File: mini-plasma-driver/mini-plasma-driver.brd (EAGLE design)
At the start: 100 x 80 mm, 92 parts, among them IC1 IR21844D, IC2 74LS19N, IC3 NE555N, IC5 IR21844D, J1 12v IN, Q1 STH60N10W, Q3 2N2369, Q4 2N2369, Q7 STH60N10W, Q8 STH60N10W, Q9 STH60N10W

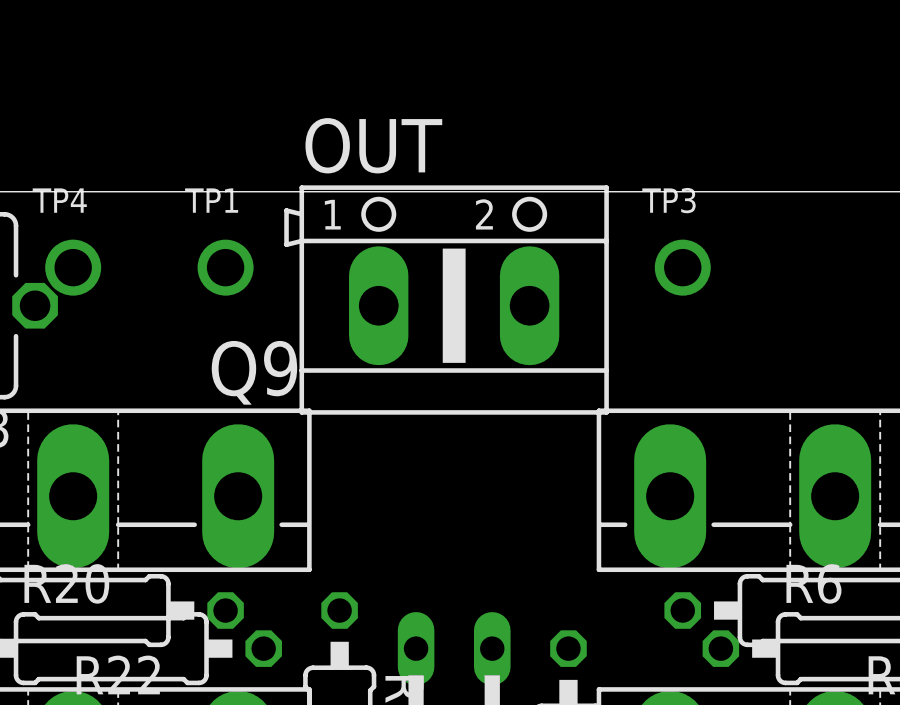
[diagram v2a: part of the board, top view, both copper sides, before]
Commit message: rotate out connector so that wires dont cross eachother
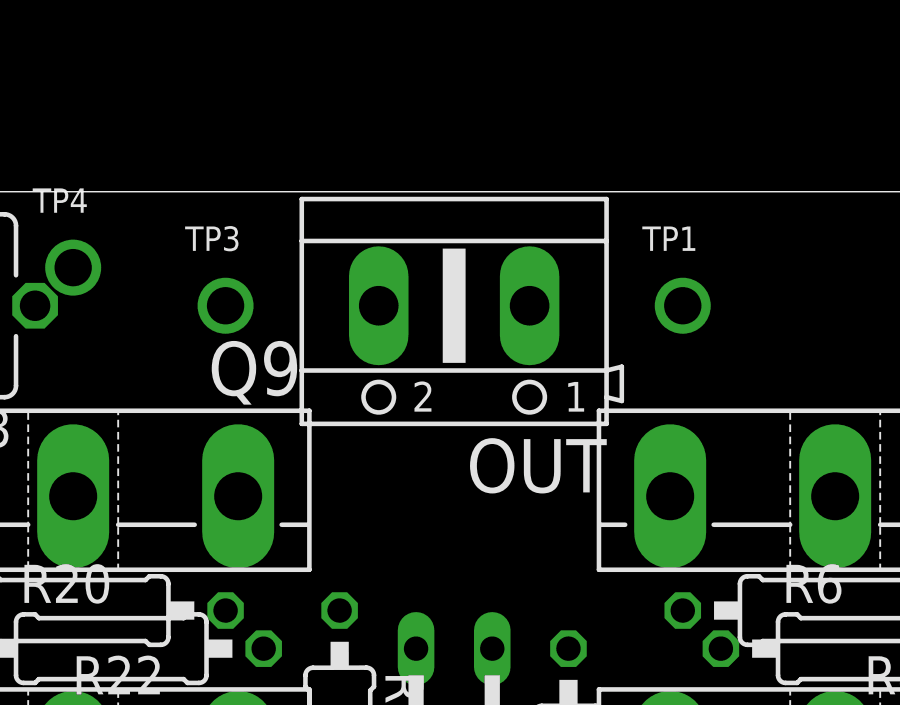
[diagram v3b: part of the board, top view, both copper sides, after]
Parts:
- moved TP1 15.3 mm to (71.1, 76.2)
- moved TP3 15.3 mm to (55.9, 76.2)
- turned OUT to 180 degrees
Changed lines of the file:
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@@
 <attribute name="OC_NEWARK" value="unknown" x="13.97" y="5.08" size="1.778" layer="28" rot="MR180" display="off"/>
 </element>
-<element name="OUT" library="con-ptr500" library_urn="urn:adsk.eagle:library:181" package="AK500/2" package3d_urn="urn:adsk.eagle:package:9880/1" value="" x="63.5" y="76.2">
-<attribute name="MF" value="" x="63.5" y="76.2" size="1.778" layer="27" display="off"/>
-<attribute name="MPN" value="" x="63.5" y="76.2" size="1.778" layer="27" display="off"/>
-<attribute name="OC_FARNELL" value="unknown" x="63.5" y="76.2" size="1.778" layer="27" display="off"/>
-<attribute name="OC_NEWARK" value="unknown" x="63.5" y="76.2" size="1.778" layer="27" display="off"/>
+<element name="OUT" library="con-ptr500" library_urn="urn:adsk.eagle:library:181" package="AK500/2" package3d_urn="urn:adsk.eagle:package:9880/1" value="" x="63.5" y="76.2" rot="R180">
+<attribute name="MF" value="" x="63.5" y="76.2" size="1.778" layer="27" rot="R180" display="off"/>
+<attribute name="MPN" value="" x="63.5" y="76.2" size="1.778" layer="27" rot="R180" display="off"/>
+<attribute name="OC_FARNELL" value="unknown" x="63.5" y="76.2" size="1.778" layer="27" rot="R180" display="off"/>
+<attribute name="OC_NEWARK" value="unknown" x="63.5" y="76.2" size="1.778" layer="27" rot="R180" display="off"/>
 </element>
 <element name="Q3" library="transistor-npn" library_urn="urn:adsk.eagle:library:398" package="TO18" package3d_urn="urn:adsk.eagle:package:28973/2" value="2N2369" x="77.47" y="8.89"/>
@@
 <attribute name="OC_NEWARK" value="29M3118" x="11.43" y="62.23" size="1.778" layer="27" rot="R180" display="off"/>
 </element>
-<element name="TP1" library="microbuilder" package="1X01_ROUND" value="" x="55.88" y="77.47">
-<attribute name="BOM" value="EXCLUDE" x="55.88" y="77.47" size="1.778" layer="27" display="off"/>
+<element name="TP1" library="microbuilder" package="1X01_ROUND" value="" x="71.12" y="76.2">
+<attribute name="BOM" value="EXCLUDE" x="71.12" y="76.2" size="1.778" layer="27" display="off"/>
 </element>
 <element name="TP11" library="microbuilder" package="1X01_ROUND" value="" x="7.62" y="77.47">
@@
 <attribute name="BOM" value="EXCLUDE" x="76.2" y="3.81" size="1.778" layer="27" display="off"/>
 </element>
-<element name="TP3" library="microbuilder" package="1X01_ROUND" value="" x="71.12" y="77.47">
-<attribute name="BOM" value="EXCLUDE" x="71.12" y="77.47" size="1.778" layer="27" display="off"/>
+<element name="TP3" library="microbuilder" package="1X01_ROUND" value="" x="55.88" y="76.2">
+<attribute name="BOM" value="EXCLUDE" x="55.88" y="76.2" size="1.778" layer="27" display="off"/>
 </element>
 <element name="TP4" library="microbuilder" package="1X01_ROUND" value="" x="50.8" y="77.47">
@@
 <wire x1="80.01" y1="45.72" x2="83.82" y2="49.53" width="0" layer="19" extent="1-1"/>
 <wire x1="76.2" y1="69.85" x2="82.55" y2="64.77" width="0" layer="19" extent="1-1"/>
-<wire x1="60.9854" y1="76.2" x2="76.2" y2="69.85" width="0" layer="19" extent="1-1"/>
-<wire x1="55.88" y1="77.47" x2="60.9854" y2="76.2" width="0" layer="19" extent="1-1"/>
+<wire x1="66.0146" y1="76.2" x2="76.2" y2="69.85" width="0" layer="19" extent="1-1"/>
+<wire x1="71.12" y1="76.2" x2="66.0146" y2="76.2" width="0" layer="19" extent="1-1"/>
 </signal>
 <signal name="COM">
@@
 <contactref element="Q8" pad="S"/>
 <contactref element="Q9" pad="D"/>
-<wire x1="66.0146" y1="76.2" x2="71.12" y2="77.47" width="0" layer="19" extent="1-1"/>
-<wire x1="57.15" y1="64.77" x2="66.0146" y2="76.2" width="0" layer="19" extent="1-1"/>
+<wire x1="60.9854" y1="76.2" x2="55.88" y2="76.2" width="0" layer="19" extent="1-1"/>
+<wire x1="57.15" y1="64.77" x2="60.9854" y2="76.2" width="0" layer="19" extent="1-1"/>
 <wire x1="56.3" y1="60.96" x2="57.15" y2="64.77" width="0" layer="19" extent="1-1"/>
 <wire x1="54.61" y1="57.15" x2="56.3" y2="60.96" width="0" layer="19" extent="1-1"/>

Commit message: some initial routing
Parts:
- moved TP11 27.2 mm to (2.03, 50.8)
- moved R12 3.56 mm to (14.0, 73.4)
- moved TP2 2.59 mm to (73.7, 3.30)
- moved CY2 2.03 mm to (13.2, 50.8), turned to 180 degrees
- moved TP5 1.85 mm to (28.7, 78.0)
- moved JP1 1.30 mm to (8.89, 67.6), turned to 180 degrees
- moved LED4_RED 0.76 mm to (10.2, 73.2)
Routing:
- net VDD-: track 0.00 -> 74.7 mm
- net 12V: track 0.00 -> 63.9 mm
- net EARTH: track 0.00 -> 58.6 mm
- net N$18: track 0.00 -> 34.2 mm
- net VDD: track 0.00 -> 28.0 mm
- net N$2: track 0.00 -> 25.2 mm
- net N$15: track 0.00 -> 24.0 mm
- net N$31: track 0.00 -> 22.0 mm
- net N$20: track 0.00 -> 21.9 mm
- net N$19: track 0.00 -> 20.8 mm
- net N$22: track 0.00 -> 20.0 mm
- net OUT555: track 0.00 -> 19.2 mm
- net N$14: track 0.00 -> 18.4 mm
- net N$16: track 0.00 -> 15.3 mm
- net N$13: track 0.00 -> 14.9 mm
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- added copper zone on layer 16, net GND

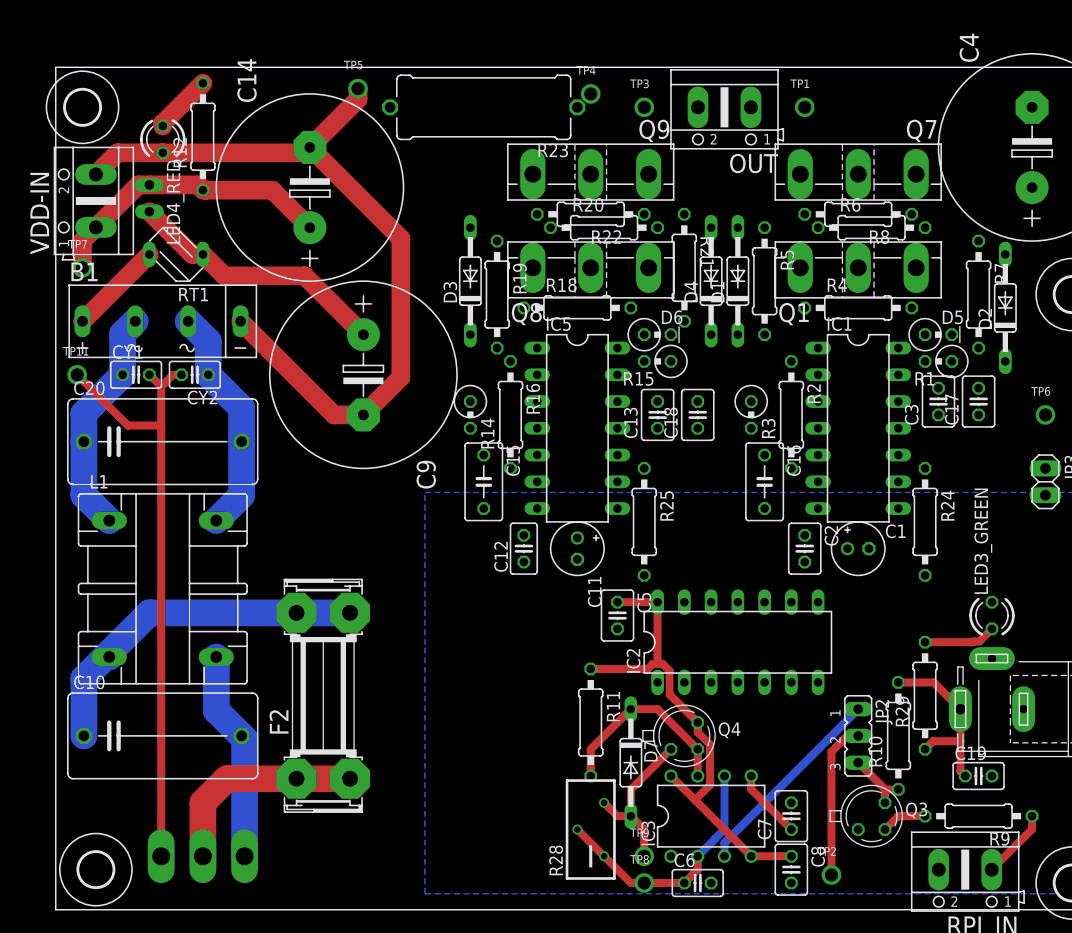
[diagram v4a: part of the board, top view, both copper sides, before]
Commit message: ver. 7/27/18 20:15 corrected L1 package; placed TP11; gave driver DIPs more space for sockets.
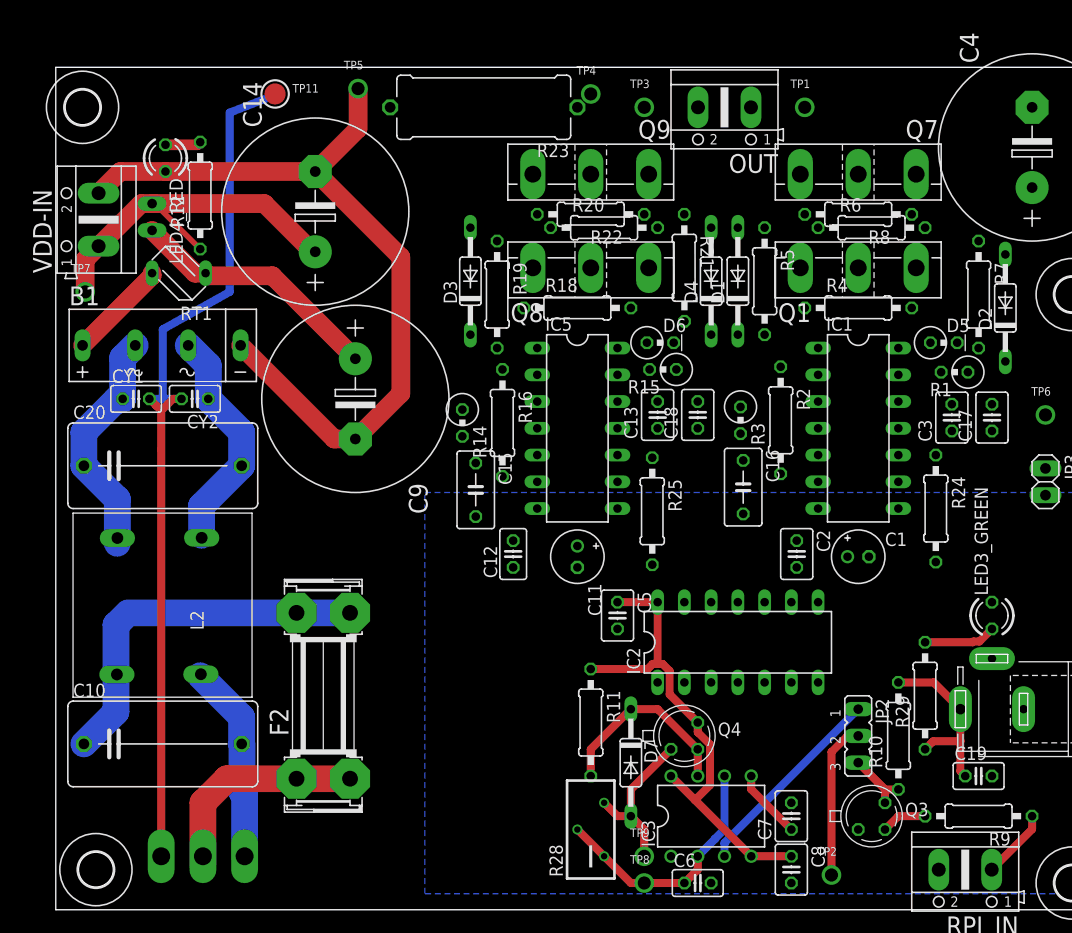
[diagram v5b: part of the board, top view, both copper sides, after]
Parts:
- removed L1: MFE, inductors:MFE
- added L2: KEMET_SC-03-10, CdF Common:KEMET_SC-03-10
- TP11: device microbuilder:1X01_ROUND -> microbuilder:TESTPOINT_ROUND_2MM
- moved TP11 32.6 mm to (20.8, 77.5)
- moved R12 5.59 mm to (13.7, 67.8)
- moved C9 2.41 mm to (28.4, 48.5)
- moved C14 2.34 mm to (24.6, 66.3)
- moved TP7 2.30 mm to (2.79, 58.7)
- moved B1 2.29 mm to (10.2, 53.6)
- moved C20 2.29 mm to (10.2, 42.2)
- moved CY1 2.29 mm to (7.62, 48.5)
- moved CY2 2.29 mm to (13.2, 48.5)
- moved C16 2.09 mm to (65.3, 40.1)
- moved C17 1.98 mm to (88.9, 46.7)
- moved C3 1.98 mm to (85.1, 46.7)
- moved R1 1.83 mm to (85.3, 51.1)
- moved LED4_RED 1.80 mm to (10.4, 71.4)
- moved VDD-IN 1.80 mm to (4.06, 65.5)
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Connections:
- net EARTH: now also TP11.P$1; no longer TP11.1
- net N$18: now also L2.3; no longer L1.1
- net N$20: now also L2.2; no longer L1.4
- net N$22: now also L2.4; no longer L1.2
- net N$31: now also L2.1; no longer L1.3
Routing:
- net EARTH: track 58.6 -> 85.1 mm
- net VDD: track 28.0 -> 35.4 mm
- net N$18: track 34.2 -> 36.9 mm
- net N$32: track 5.64 -> 3.41 mm
- net VDD-: track 74.7 -> 76.1 mm
- net N$22: track 20.0 -> 18.9 mm
- net N$2: track 25.2 -> 24.4 mm
- net N$25: track 8.98 -> 9.59 mm

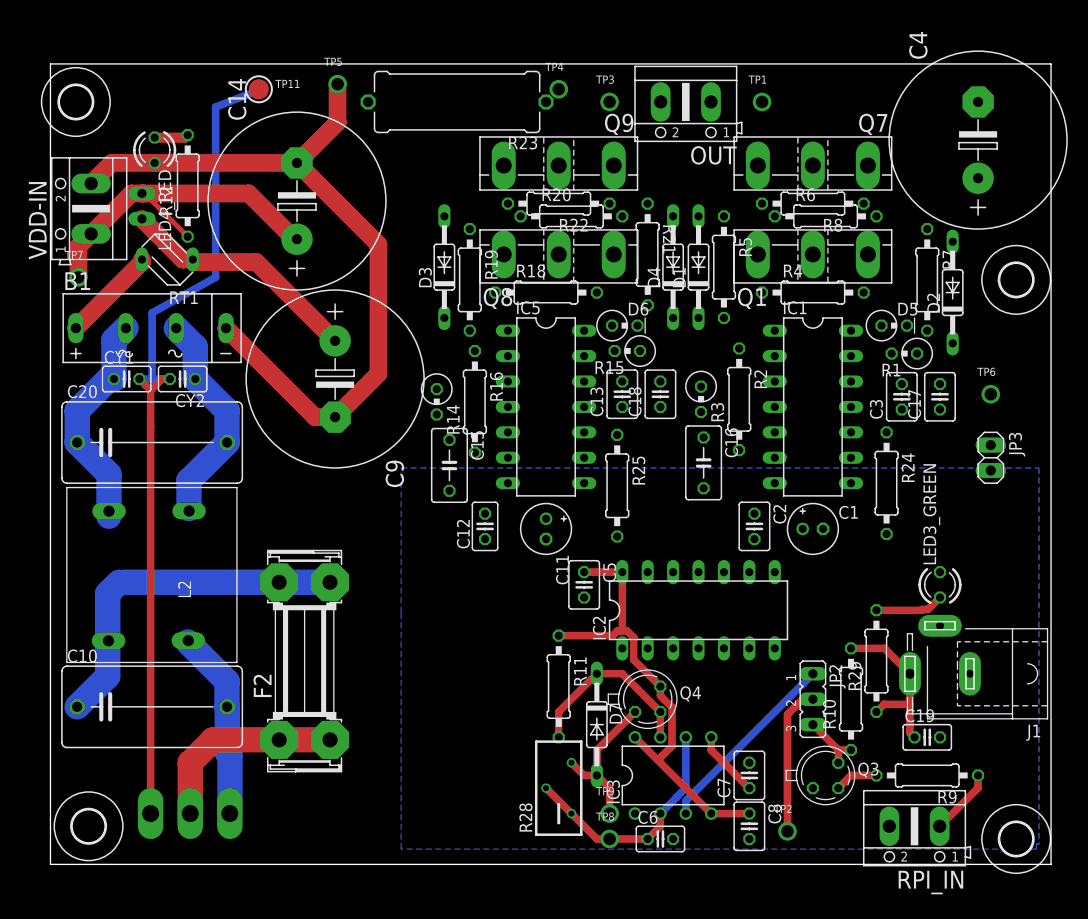
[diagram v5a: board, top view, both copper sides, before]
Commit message: Rotated driver chips and compleeted routing; Still have air wires remaining. Unclear what else need to be done.
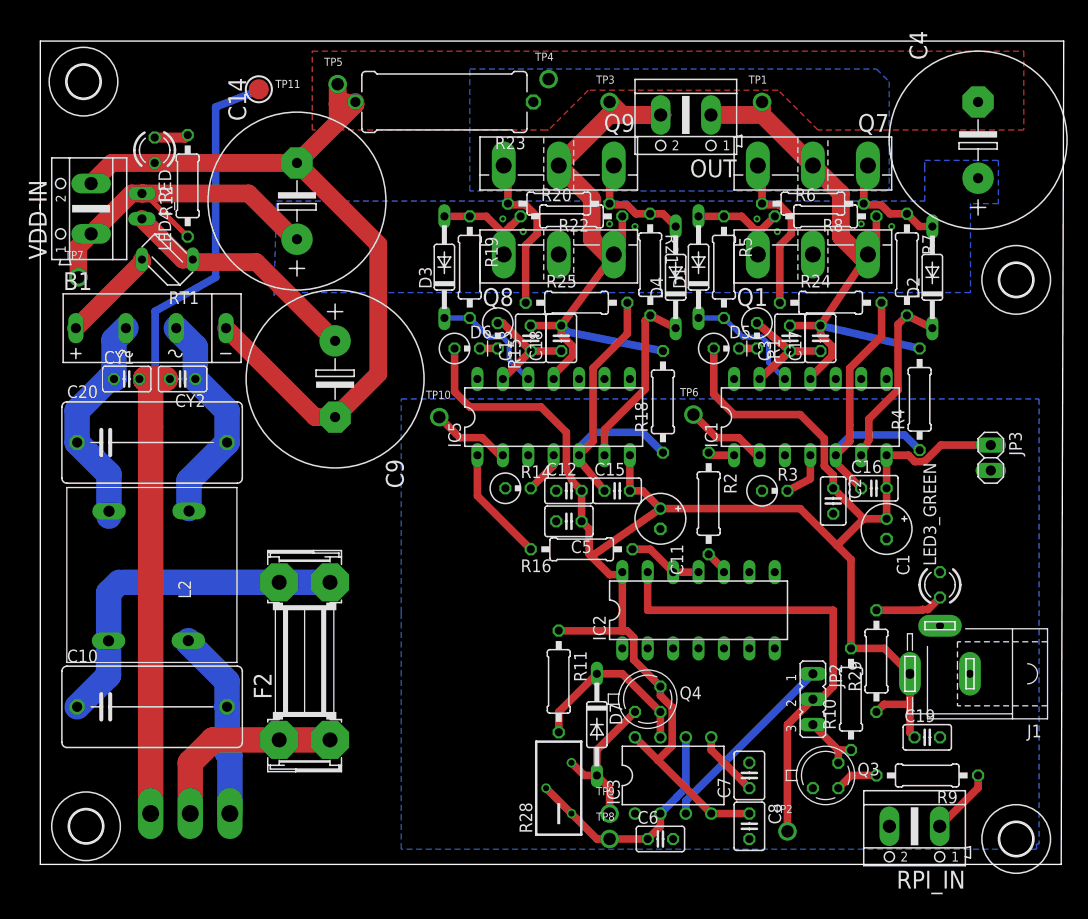
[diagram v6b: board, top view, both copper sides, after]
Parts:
- added TP10: (no value), microbuilder:1X01_ROUND
- C15, C16: device rcl:C050-035X075 -> rcl:C025-025X050
- C2: device rcl:C025-030X050 -> rcl:C025-025X050
- moved TP6 29.8 mm to (64.3, 45.0)
- moved R24 18.9 mm to (78.0, 56.1), turned to 0 degrees
- moved R25 18.7 mm to (52.6, 56.1), turned to 0 degrees
- moved R16 18.2 mm to (53.1, 31.5), turned to 0 degrees
- moved C16 17.2 mm to (82.3, 37.6), turned to 0 degrees
- moved C15 17.0 mm to (56.6, 37.3), turned to 0 degrees
- moved D5 16.9 mm to (67.6, 51.6)
- moved R18 16.0 mm to (61.2, 46.2), turned to 90 degrees
- moved D6 15.9 mm to (41.7, 51.6)
- moved R4 15.1 mm to (86.9, 46.5), turned to 90 degrees
- moved R1 14.8 mm to (70.6, 52.8), turned to 270 degrees
- moved C17 13.3 mm to (77.0, 52.6)
- moved R15 13.0 mm to (44.7, 52.8), turned to 270 degrees
- moved C3 12.6 mm to (73.9, 52.6)
- moved R14 11.9 mm to (46.7, 37.6), turned to 0 degrees
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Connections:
- net N$35 renamed COMMON
- net VDD renamed VDD+
- removed net COM: C15.1, C16.1, IC1.5, IC5.5, R18.1, R24.2, R25.2, R4.1
- removed net N$24: IC2.10, R16.2
- removed net VB: C13.1, C17.1, C18.1, C3.1, IC1.13, IC5.13, R1.1, R15.1
- new net COM1: C16.1, IC1.5, R24.2, R4.1
- new net COM2: C15.1, IC5.5, R18.1, R25.2
- new net N$33: IC5.2, TP10.1
- new net N$36: IC2.11, IC2.12, R16.2
- new net VB1: C17.1, C3.1, IC1.13, R1.1
- new net VB2: C13.1, C18.1, IC5.13, R15.1
- net N$4: now also IC2.10; no longer IC2.11, IC2.12
- net SD: no longer IC5.2
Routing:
- net 12V: track 63.9 -> 190.9 mm
- net O2: track 0.00 -> 63.6 mm
- net O1: track 0.00 -> 58.4 mm
- net COMMON: track 0.00 -> 33.2 mm
- net COM2: track 0.00 -> 32.3 mm
- net N$13: track 14.9 -> 46.8 mm
- net COM1: track 0.00 -> 31.8 mm
- net N$29: track 0.00 -> 18.7 mm
- net N$8: track 0.00 -> 18.6 mm
- net N$7: track 0.00 -> 13.6 mm
- net N$28: track 0.00 -> 13.3 mm
- net N$5: track 0.00 -> 12.3 mm
- net N$27: track 0.00 -> 11.9 mm
- net N$9: track 0.00 -> 11.8 mm
- net N$23: track 0.00 -> 11.6 mm
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- added copper zone on layer 16, net COMMON
- added copper zone on layer 16, net VDD+
- added copper zone on layer 1, net VDD-
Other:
- board size 100 x 80 mm -> 102.3 x 82.3 mm
